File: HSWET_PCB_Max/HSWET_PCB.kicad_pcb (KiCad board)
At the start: 2 copper layers, 105 x 100.2 mm, 21 parts, among them IC3 PS2565L-1-V-F3-A, IC4 PS2565L-1-V-F3-A, IC5 PS2565L-1-V-F3-A, J1 CON-SOCJ-2155, J2 Conn_01x05, J3 CON-SOCJ-2155, U1 INA260AIPWR, U2 YAAJ_DCDC_StepDown_LM2596, U3 YAAJ_DCDC_StepDown_LM2596

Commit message: routing done
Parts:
- A1: footprint Module:Arduino_UNO_R3 -> footprints.:ARDUINO_ARDUINO_UNO_REV3
- S1: moved to B.Cu
- moved J1 105.8 mm to (80.3, 67.9), turned to -90 degrees
- moved U3 66.6 mm to (78.8, 118.2), turned to 180 degrees
- moved A1 65.2 mm to (113.7, 92.8), turned to 90 degrees
- moved R4 56.3 mm to (83.0, 96.8), turned to 90 degrees
- moved IC3 55.6 mm to (77.7, 100.8), turned to 90 degrees
- moved R8 50.4 mm to (83.0, 81.4), turned to 90 degrees
- moved R1 47.3 mm to (83.0, 104.3), turned to 90 degrees
- moved IC4 46.4 mm to (77.5, 85.2), turned to 90 degrees
- moved U2 41.5 mm to (149.5, 122.5), turned to 180 degrees
- moved R2 39.9 mm to (83.0, 88.8)
- moved J3 33.4 mm to (155.0, 66.0), turned to -90 degrees
- moved C1 26.0 mm to (147.0, 78.2), turned to 0 degrees
- moved R5 22.5 mm to (154.5, 78.5), turned to -90 degrees
- moved S1 22.1 mm to (162.0, 88.0)
- moved D2 20.6 mm to (163.0, 104.3), turned to 90 degrees
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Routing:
- net Turbine_PWR: track 0.00 -> 129.5 mm
- net Net-(U2-Vin): track 0.00 -> 114.4 mm
- net Turbine_Encoder: track 0.00 -> 98.6 mm, vias 0 -> 2
- net A4: track 0.00 -> 41.1 mm, vias 0 -> 4
- net arduino_lin_act: track 0.00 -> 30.6 mm, vias 0 -> 2
- net A5: track 0.00 -> 28.2 mm
- net arduino_encoder: track 0.00 -> 23.7 mm, vias 0 -> 2
- net 6V: track 0.00 -> 19.6 mm
- net 5V: track 0.00 -> 19.0 mm, vias 0 -> 12
- net 9V: track 0.00 -> 14.0 mm
- net Net-(IC4-CATHODE_ANODE): track 0.00 -> 4.70 mm
- net Net-(IC3-CATHODE_ANODE): track 0.00 -> 4.21 mm
- net Sensor_PWR: track 0.00 -> 3.68 mm
- net Net-(IC5-CATHODE_ANODE): track 0.00 -> 3.43 mm
- added copper zone on B.Cu, net 5V
- added copper zone on F.Cu, net GND
- removed copper zone on B.Cu, net GND
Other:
- board size 105 x 100.2 mm -> 138.5 x 86 mm

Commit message: Integrated safety
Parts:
- added C2: 0.47, footprints:CAPPRD500W60D1000H3150, F.Cu at (174.3, 102.4)
- added C3: 10u, Capacitor_SMD:C_0603_1608Metric, B.Cu at (142.0, 101.9)
- added D1: STPS120M, footprints:DIO_STPS1L40M, B.Cu at (149.4, 114.0)
- added L1: 10u, Inductor_SMD:L_0603_1608Metric, B.Cu at (142.0, 105.2)
- added R9: 10, Resistor_SMD:R_2512_6332Metric, B.Cu at (143.4, 111.0)
- added U4: LTC3525ESC6-5-TRMPBF, footprints:SC70-SC6_LIT, B.Cu at (145.6, 103.2)
- added U5: SN74HC14N, footprints:D14, B.Cu at (154.5, 106.8)
- moved U3 95.9 mm to (174.6, 122.4)
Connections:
- A1 pad D4: unconnected-(A1-PadD4) -> Safety Signal
- D2 pad 1: Turbine_PWR -> Turbine_PWR_Sensed
- IC5 pad 1: Turbine_PWR -> Turbine_PWR_Sensed
- S1 pad 3: Turbine_PWR -> Turbine_PWR_Sensed
- U1 pad 14: Turbine_PWR -> Turbine_PWR_Sensed
- U1 pad 15: Turbine_PWR -> Turbine_PWR_Sensed
- U1 pad 16: Turbine_PWR -> Turbine_PWR_Sensed
- U3 pad 4: 5V -> 5V_BUCK
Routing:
- net Safety Signal: track 0.00 -> 77.2 mm
- net Net-(U2-Vin): track 114.4 -> 62.0 mm
- net Net-(U4-*SHDN): track 0.00 -> 44.2 mm
- net 5V_BUCK: track 0.00 -> 27.3 mm, vias 0 -> 1
- net GND: track 0.00 -> 6.53 mm, vias 0 -> 3
- net 5V: track 19.0 -> 24.7 mm, vias 12 -> 13
- net Net-(U4-SW): track 0.00 -> 4.84 mm
- net Net-(D1-K): track 0.00 -> 4.51 mm

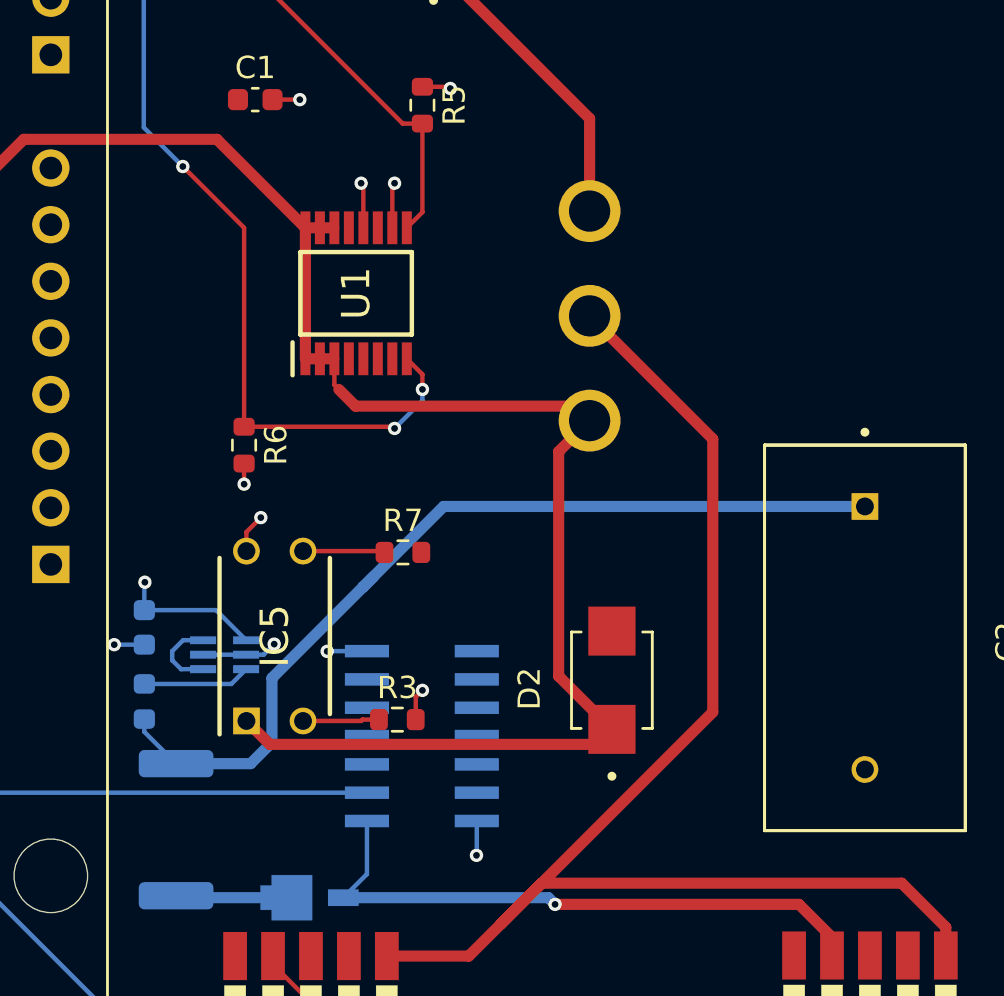
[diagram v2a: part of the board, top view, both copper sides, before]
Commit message: Completed layout for safety system
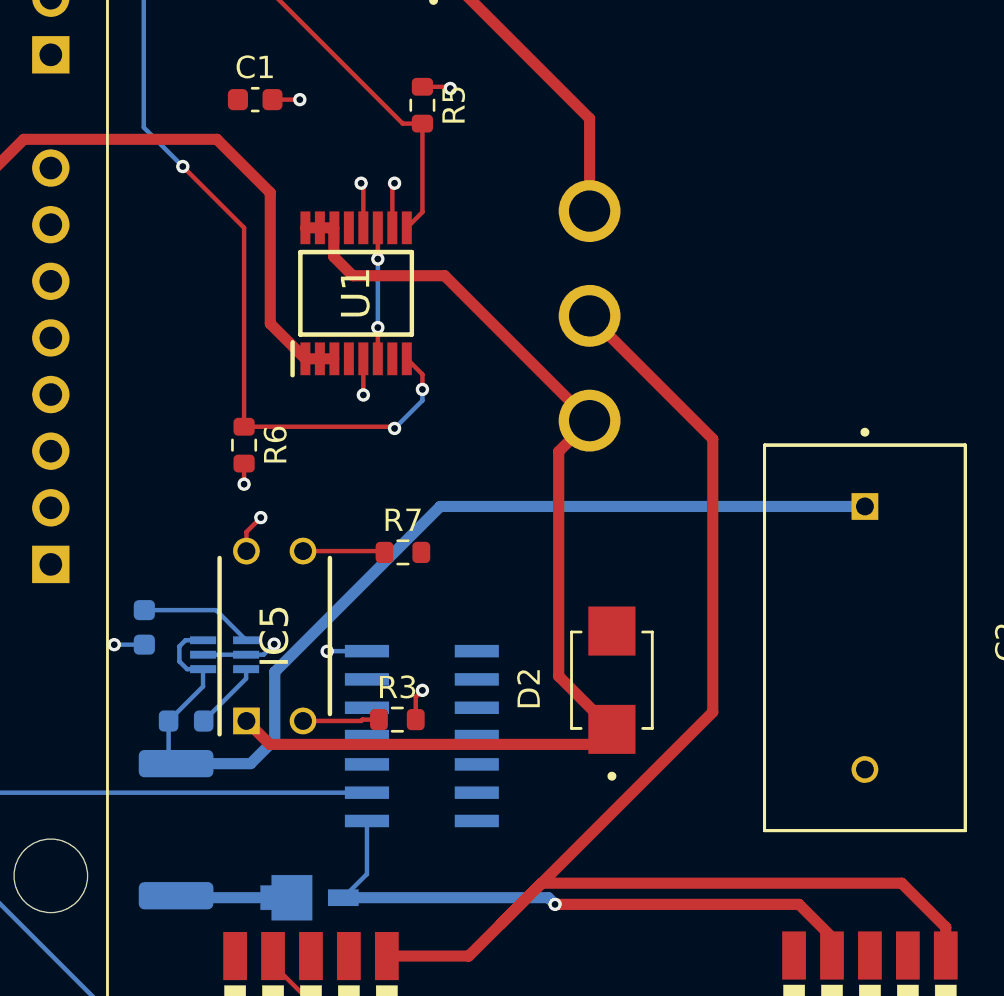
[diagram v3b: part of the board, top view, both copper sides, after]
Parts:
- U1: footprint footprints.:ina260 -> footprints:ina260
- moved L1 2.07 mm to (143.9, 106.1), turned to 0 degrees
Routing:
- net Turbine_PWR_Sensed: track 0.00 -> 49.6 mm
- net Turbine_PWR: track 129.5 -> 82.4 mm
- net GND: track 6.53 -> 14.3 mm, vias 3 -> 6
- net 5V: track 24.7 -> 21.9 mm, vias 13 -> 11
- net Net-(U4-SW): track 4.84 -> 3.11 mm
- net Net-(U4-*SHDN): track 44.2 -> 45.5 mm

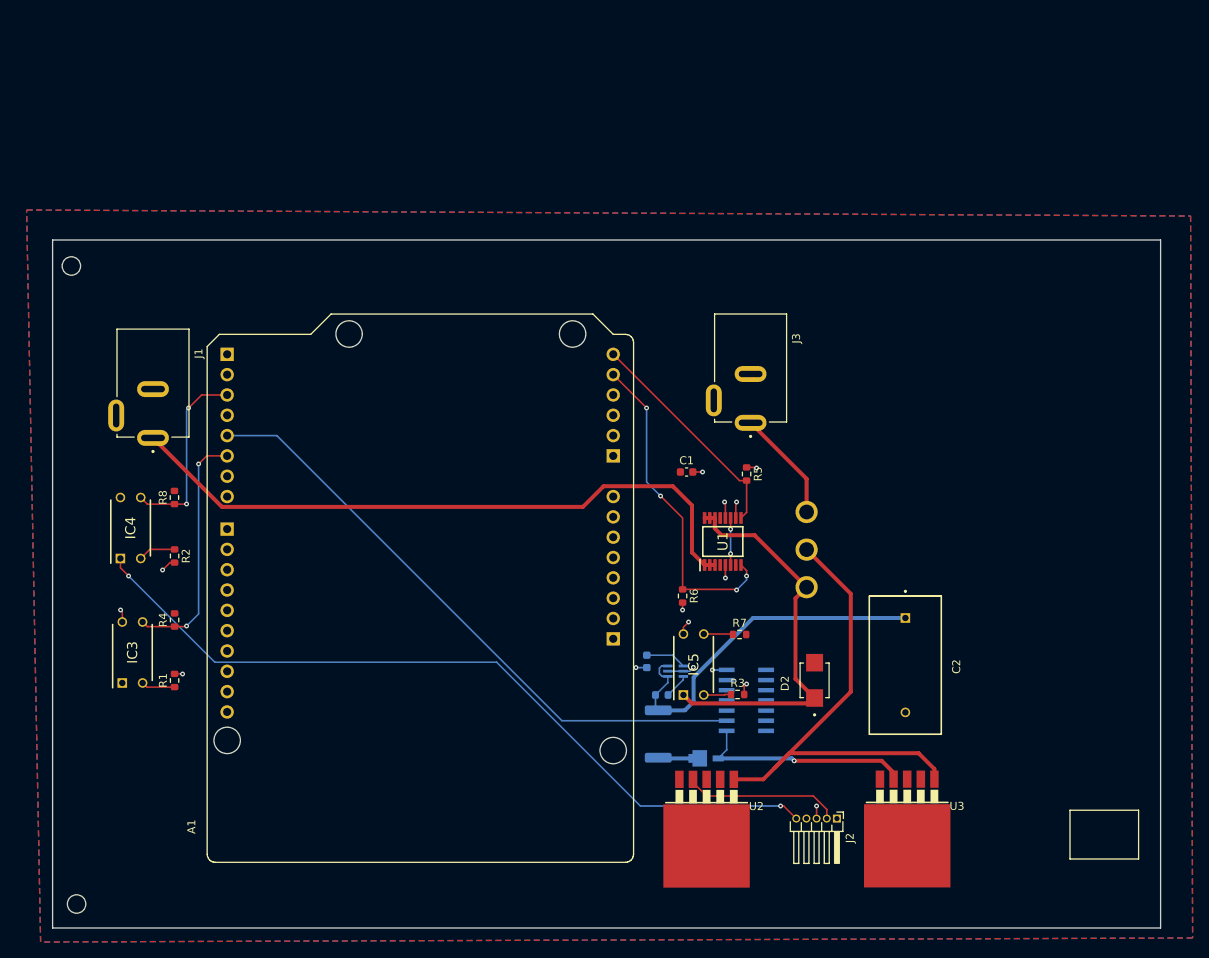
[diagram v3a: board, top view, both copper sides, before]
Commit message: added maybe unecessary plane, swapped 1x05 connector -> 1x04 after mirabel got rid of 6v, ficed footprint for lm2596
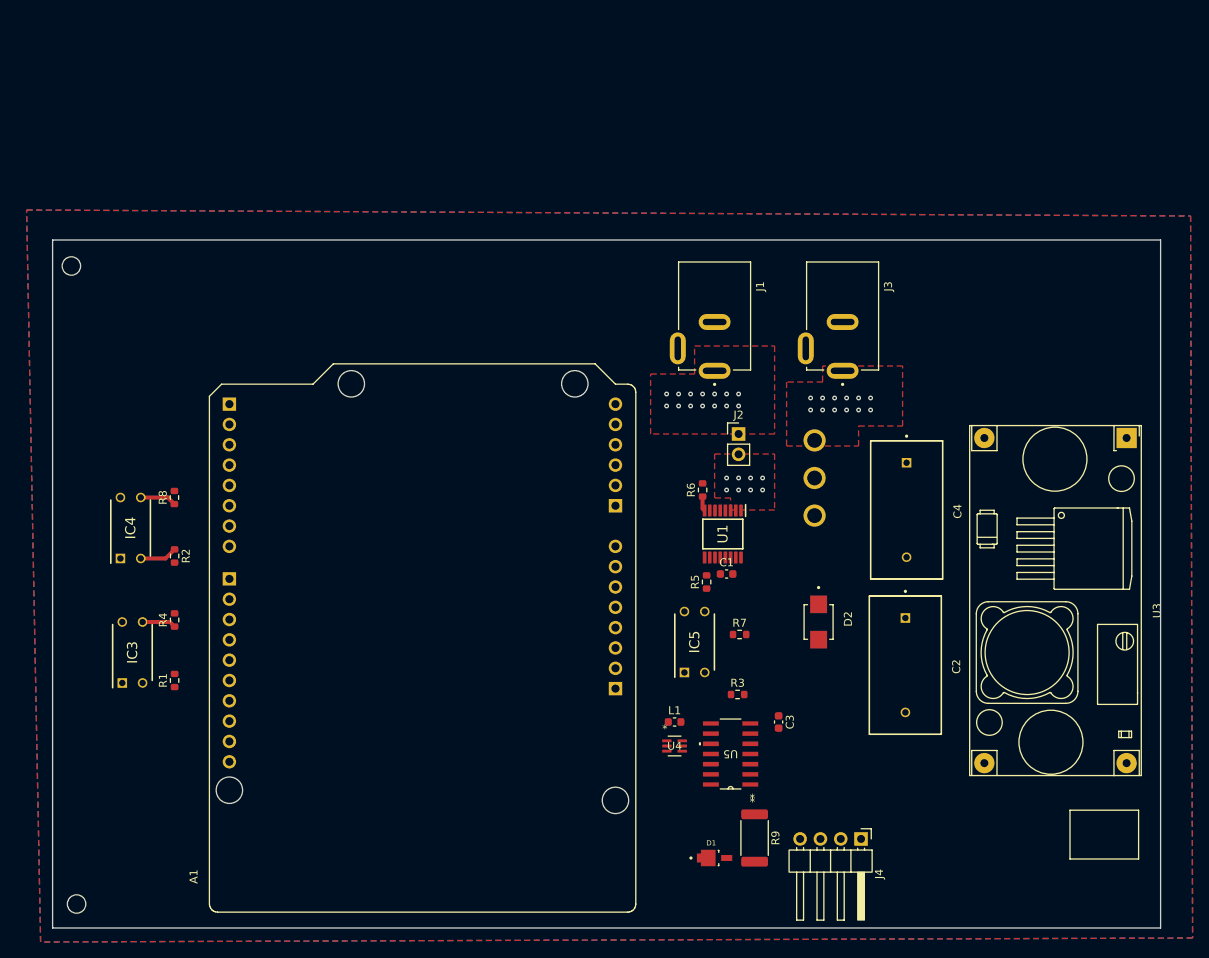
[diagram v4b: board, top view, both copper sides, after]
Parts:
- removed U2: YAAJ_DCDC_StepDown_LM2596, footprints:TO263-5
- added C4: 0.47, footprints:CAPPRD500W60D1000H3150, F.Cu at (174.5, 83.0)
- added J4: turbine bus, Connector_PinHeader_2.54mm:PinHeader_1x04_P2.54mm_Horizontal, F.Cu at (168.8, 124.1)
- C3, D1, L1, R9, U4, U5: moved to F.Cu
- J2: value Conn_01x05 -> emergency stop; footprint Connector_PinHeader_1.27mm:PinHeader_1x05_P1.27mm_Horizontal -> Connector_PinHeader_2.54mm:PinHeader_1x02_P2.54mm_Vertical
- U3: footprint footprints:TO263-5 -> footprints:YAAJ_DCDC_StepDown_LM2596
- moved J1 70.7 mm to (150.5, 59.5)
- moved U3 55.7 mm to (202.0, 74.0), turned to -90 degrees
- moved J2 49.6 mm to (153.5, 73.5), turned to 0 degrees
- moved C3 18.1 mm to (158.5, 109.5)
- moved R9 17.7 mm to (155.5, 124.0), turned to -90 degrees
- moved R5 14.4 mm to (149.5, 92.0), turned to 90 degrees
- moved C1 13.7 mm to (152.0, 91.0)
- moved R6 13.5 mm to (149.0, 80.5), turned to 90 degrees
- moved J3 13.2 mm to (166.5, 59.5)
- moved D1 12.5 mm to (150.5, 126.5)
- moved U4 9.35 mm to (145.5, 112.5)
- moved S1 9.01 mm to (163.0, 79.0)
- moved D2 7.31 mm to (163.5, 97.0), turned to -90 degrees
- moved U5 6.99 mm to (152.5, 113.5), turned to 180 degrees
- moved A1 6.23 mm to (114.0, 99.0)
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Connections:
- C2 pad 1: Net-(U4-*SHDN) -> Net-(D1-K)
- D1 pad 2: 5V_BUCK -> Net-(D1-A)
- J2 pad 1: GND -> Turbine_PWR
- J2 pad 2: 6V -> Turbine_PWR_Safety
- L1 pad 1: Net-(U4-*SHDN) -> Net-(D1-K)
- R9 pad 1: Net-(D1-K) -> 4.5V_BUCK
- R9 pad 2: Net-(U4-*SHDN) -> Net-(D1-A)
- U1 pad 1: Turbine_PWR -> Turbine_PWR_Safety
- U1 pad 2: Turbine_PWR -> Turbine_PWR_Safety
- U1 pad 3: Turbine_PWR -> Turbine_PWR_Safety
- U3 pad 4: 5V_BUCK -> 4.5V_BUCK
- U4 pad 1: Net-(U4-*SHDN) -> Net-(D1-K)
- U4 pad 3: Net-(U4-*SHDN) -> Net-(D1-K)
- U5 pad 1: 5V_BUCK -> 4.5V_BUCK
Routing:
- net Turbine_Encoder: track 98.6 -> 0.00 mm, vias 2 -> 0
- net Turbine_PWR: track 82.4 -> 0.00 mm, vias 0 -> 14
- net Safety Signal: track 77.2 -> 0.00 mm
- net Net-(U3-Vin): track 62.0 -> 0.00 mm
- net Turbine_PWR_Sensed: track 49.6 -> 0.00 mm
- net Net-(U4-*SHDN): track 45.5 -> 0.00 mm
- net A4: track 41.1 -> 1.83 mm, vias 4 -> 0
- net A5: track 28.2 -> 0.00 mm
- net 5V_BUCK: track 27.3 -> 0.00 mm, vias 1 -> 0
- net arduino_lin_act: track 30.6 -> 4.24 mm, vias 2 -> 0
- net 5V: track 21.9 -> 0.00 mm, vias 11 -> 0
- net 6V: track 19.6 -> 0.00 mm
- net arduino_encoder: track 23.7 -> 4.55 mm, vias 2 -> 0
- net GND: track 14.3 -> 0.00 mm, vias 6 -> 0
- net 9V: track 14.0 -> 0.00 mm, vias 0 -> 12
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- added copper zone on F.Cu, net 9V
- added copper zone on F.Cu, net Turbine_PWR
- added copper zone on F.Cu, net Turbine_PWR_Safety

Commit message: new routing for pcb, some smaller ports still unrouted
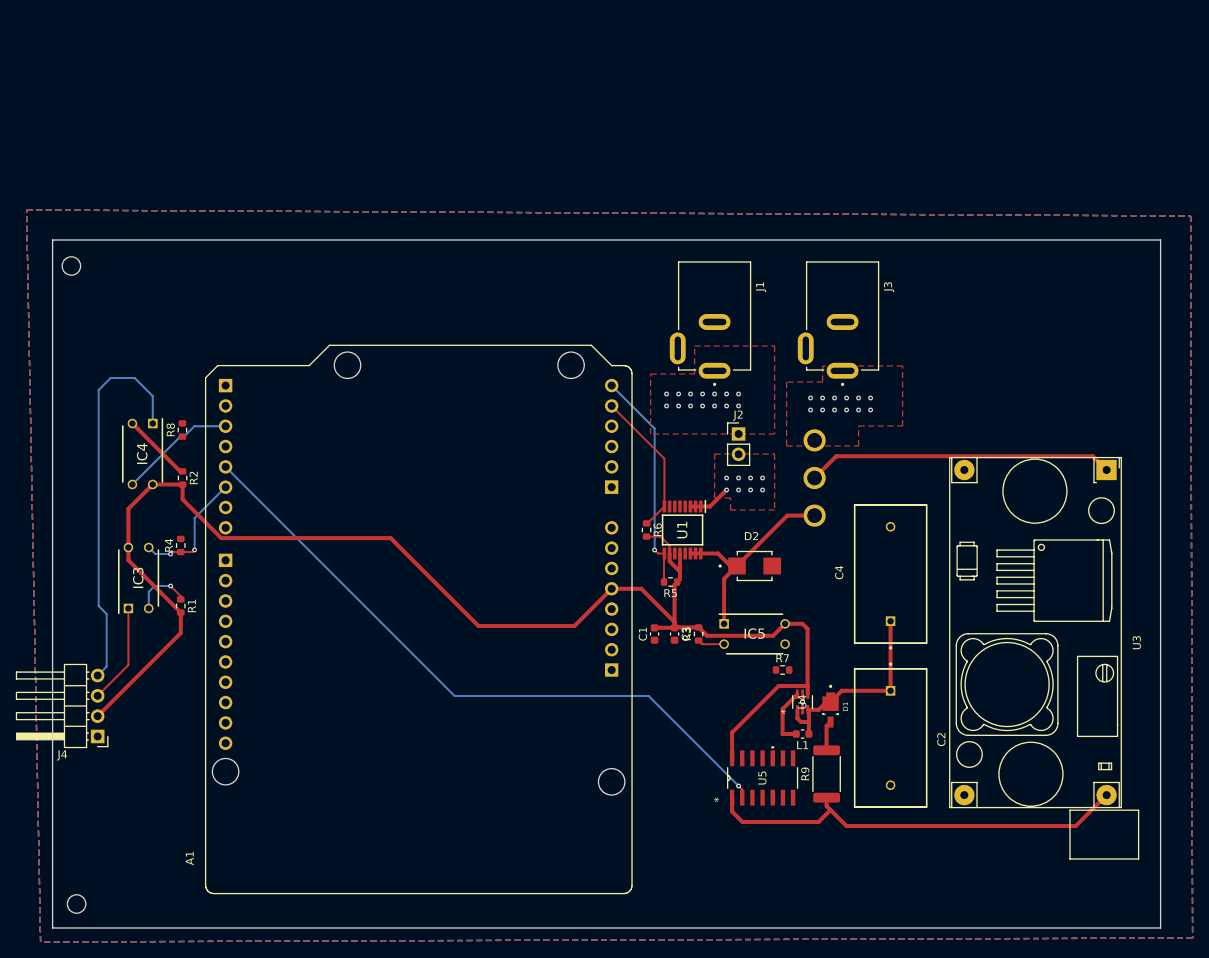
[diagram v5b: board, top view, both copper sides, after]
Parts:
- moved J4 96.3 mm to (73.4, 111.3), turned to 180 degrees
- moved D1 23.5 mm to (165.0, 108.0), turned to -90 degrees
- moved C3 17.0 mm to (145.5, 98.5)
- moved U4 16.9 mm to (161.5, 107.0), turned to 90 degrees
- moved L1 16.1 mm to (161.5, 111.0), turned to 180 degrees
- moved R9 12.0 mm to (164.5, 116.0), turned to 90 degrees
- moved C1 11.7 mm to (143.0, 98.5), turned to 90 degrees
- moved D2 10.6 mm to (155.5, 90.0), turned to 0 degrees
- moved R2 9.80 mm to (84.0, 79.0)
- moved IC4 9.37 mm to (79.0, 76.0), turned to -90 degrees
- moved IC3 9.34 mm to (78.5, 91.5)
- moved R1 9.34 mm to (83.8, 95.0), turned to -90 degrees
- moved R4 9.34 mm to (83.8, 87.4)
- moved C2 9.29 mm to (172.5, 111.5)
- moved R3 9.00 mm to (148.5, 98.5), turned to 90 degrees
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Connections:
- J4 pad 3: turbine_lin_act -> Turbine_lin_act
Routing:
- net 5V: track 0.00 -> 175.6 mm
- net Safety Signal: track 0.00 -> 82.3 mm, vias 0 -> 1
- net 4.5V_BUCK: track 0.00 -> 53.9 mm
- net Turbine_Encoder: track 0.00 -> 48.3 mm
- net Net-(U3-Vin): track 0.00 -> 38.3 mm
- net A5: track 0.00 -> 27.8 mm, vias 0 -> 1
- net Turbine_PWR_Sensed: track 0.00 -> 26.7 mm
- net Net-(D1-K): track 0.00 -> 25.8 mm
- net A4: track 1.83 -> 18.4 mm
- net Turbine_lin_act: track 0.00 -> 12.5 mm
- net arduino_lin_act: track 4.24 -> 15.7 mm, vias 0 -> 2
- net arduino_encoder: track 4.55 -> 14.9 mm
- net Net-(U4-SW): track 0.00 -> 7.44 mm
- net Net-(IC3-CATHODE_ANODE): track 0.00 -> 7.31 mm, vias 0 -> 1
- net Turbine_PWR_Safety: track 0.00 -> 5.38 mm
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- added copper zone on B.Cu, net GND

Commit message: added diagrams and small changes
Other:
- board text added: "3V3"
- board text added: "4.5V OUT"
- board text added: "5V"
- board text added: "9V TEST Power"
- board text added: "A0"
- board text added: "A1"
- board text added: "A2"
- board text added: "A3"
- board text added: "A4"
- board text added: "A4_SDA"
- board text added: "A5"
- board text added: "A5_SCL"
- board text added: "AREF"
- board text added: "Arduino UNO R3"
- board text added: "Buck Converter (steps down to 4.5V)"
- board text added: "D0"
- board text added: "D1"
- board text added: "D10"
- board text added: "D11"
- board text added: "D12"
- board text added: "D13"
- board text added: "D2"
- board text added: "D3"
- board text added: "D4"
- board text added: "D5"
- board text added: "D6"
- board text added: "D7"
- board text added: "D8"
- board text added: "D9"
- board text added: "Encoder Opto"
- board text added: "GND"
- board text added: "INA260"
- board text added: "IOREF"
- board text added: "LTC3525"
- board text added: "Linear Actuator Opto"
- board text added: "P1"
- board text added: "Power Opto"
- board text added: "RST"
- board text added: "SN74HC14N"
- board text added: "Schmitt Trigger"
- board text added: "Turbine Encoder"
- board text added: "Turbine Linear Actuator"
- board text added: "Turbine Power"
- board text added: "VIN"
